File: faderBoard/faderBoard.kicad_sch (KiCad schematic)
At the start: 22 parts, among them J1 Conn_01x14_Pin, J2 Conn_01x14_Socket, U1 ADS1115IDGS

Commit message: added footprints
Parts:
- C1, C2, C3, C4, C5: footprint (none) -> Capacitor_SMD:C_0805_2012Metric_Pad1.18x1.45mm_HandSolder
- J1: footprint (none) -> Connector_PinHeader_2.54mm:PinHeader_1x14_P2.54mm_Horizontal
- J2: footprint (none) -> Connector_PinSocket_2.54mm:PinSocket_1x14_P2.54mm_Horizontal
- JP1, JP10, JP2, JP3, JP4, JP5, JP6, JP7, JP8, JP9: footprint (none) -> Jumper:SolderJumper-2_P1.3mm_Open_RoundedPad1.0x1.5mm
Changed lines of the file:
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@@
       (effects (font (size 1.27 1.27)))
     )
-    (property "Footprint" "" (at 185.42 52.07 0)
+    (property "Footprint" "Jumper:SolderJumper-2_P1.3mm_Open_RoundedPad1.0x1.5mm" (at 185.42 52.07 0)
       (effects (font (size 1.27 1.27)) hide)
     )
@@
   (symbol (lib_id "power:VCC") (at 189.23 41.91 270) (unit 1)
     (in_bom yes) (on_board yes) (dnp no) (fields_autoplaced)
-    (property "Reference" "VCC03" (at 185.42 41.91 0)
+    (property "Reference" "#VCC03" (at 185.42 41.91 0)
       (effects (font (size 1.27 1.27)) hide)
     )
@@
       (project "faderBoard"
         (path "/8d3b36b6-6263-45d8-854a-5aadc803e839"
-          (reference "VCC03") (unit 1)
+          (reference "#VCC03") (unit 1)
         )
       )
@@
       (effects (font (size 1.27 1.27)))
     )
-    (property "Footprint" "" (at 85.09 83.82 0)
+    (property "Footprint" "Jumper:SolderJumper-2_P1.3mm_Open_RoundedPad1.0x1.5mm" (at 85.09 83.82 0)
       (effects (font (size 1.27 1.27)) hide)
     )
@@
       (effects (font (size 1.27 1.27)))
     )
-    (property "Footprint" "" (at 85.09 73.66 0)
+    (property "Footprint" "Jumper:SolderJumper-2_P1.3mm_Open_RoundedPad1.0x1.5mm" (at 85.09 73.66 0)
       (effects (font (size 1.27 1.27)) hide)
     )
@@
       (effects (font (size 1.27 1.27)))
     )
-    (property "Footprint" "" (at 185.42 30.48 0)
+    (property "Footprint" "Jumper:SolderJumper-2_P1.3mm_Open_RoundedPad1.0x1.5mm" (at 185.42 30.48 0)
       (effects (font (size 1.27 1.27)) hide)
     )
@@
   (symbol (lib_id "power:VCC") (at 137.16 26.67 0) (unit 1)
     (in_bom yes) (on_board yes) (dnp no) (fields_autoplaced)
-    (property "Reference" "VCC02" (at 137.16 30.48 0)
+    (property "Reference" "#VCC02" (at 137.16 30.48 0)
       (effects (font (size 1.27 1.27)) hide)
     )
@@
       (project "faderBoard"
         (path "/8d3b36b6-6263-45d8-854a-5aadc803e839"
-          (reference "VCC02") (unit 1)
+          (reference "#VCC02") (unit 1)
         )
       )
@@
       (effects (font (size 1.27 1.27)))
     )
-    (property "Footprint" "" (at 185.42 36.83 0)
+    (property "Footprint" "Jumper:SolderJumper-2_P1.3mm_Open_RoundedPad1.0x1.5mm" (at 185.42 36.83 0)
       (effects (font (size 1.27 1.27)) hide)
     )
@@
       (effects (font (size 1.27 1.27)) (justify left))
     )
-    (property "Footprint" "" (at 194.31 101.6 0)
+    (property "Footprint" "Connector_PinSocket_2.54mm:PinSocket_1x14_P2.54mm_Horizontal" (at 194.31 101.6 0)
       (effects (font (size 1.27 1.27)) hide)
     )
@@
       (effects (font (size 1.27 1.27)) (justify left))
     )
-    (property "Footprint" "" (at 51.7652 114.3 0)
+    (property "Footprint" "Capacitor_SMD:C_0805_2012Metric_Pad1.18x1.45mm_HandSolder" (at 51.7652 114.3 0)
       (effects (font (size 1.27 1.27)) hide)
     )
@@
       (effects (font (size 1.27 1.27)))
     )
-    (property "Footprint" "" (at 185.42 41.91 0)
+    (property "Footprint" "Jumper:SolderJumper-2_P1.3mm_Open_RoundedPad1.0x1.5mm" (at 185.42 41.91 0)
       (effects (font (size 1.27 1.27)) hide)
     )
@@
       (effects (font (size 1.27 1.27)) (justify left))
     )
-    (property "Footprint" "" (at 51.7652 38.1 0)
+    (property "Footprint" "Capacitor_SMD:C_0805_2012Metric_Pad1.18x1.45mm_HandSolder" (at 51.7652 38.1 0)
       (effects (font (size 1.27 1.27)) hide)
     )
@@
   (symbol (lib_id "power:VCC") (at 38.1 43.18 0) (unit 1)
     (in_bom yes) (on_board yes) (dnp no) (fields_autoplaced)
-    (property "Reference" "VCC" (at 38.1 46.99 0)
+    (property "Reference" "#VCC0101" (at 38.1 46.99 0)
       (effects (font (size 1.27 1.27)) hide)
     )
@@
       (project "faderBoard"
         (path "/8d3b36b6-6263-45d8-854a-5aadc803e839"
-          (reference "VCC") (unit 1)
+          (reference "#VCC0101") (unit 1)
         )
       )
@@
       (effects (font (size 1.27 1.27)))
     )
-    (property "Footprint" "" (at 85.09 78.74 0)
+    (property "Footprint" "Jumper:SolderJumper-2_P1.3mm_Open_RoundedPad1.0x1.5mm" (at 85.09 78.74 0)
       (effects (font (size 1.27 1.27)) hide)
     )
@@
       (effects (font (size 1.27 1.27)))
     )
-    (property "Footprint" "" (at 158.75 101.6 0)
+    (property "Footprint" "Connector_PinHeader_2.54mm:PinHeader_1x14_P2.54mm_Horizontal" (at 158.75 101.6 0)
       (effects (font (size 1.27 1.27)) hide)
     )
@@
       (effects (font (size 1.27 1.27)))
     )
-    (property "Footprint" "" (at 85.09 88.9 0)
+    (property "Footprint" "Jumper:SolderJumper-2_P1.3mm_Open_RoundedPad1.0x1.5mm" (at 85.09 88.9 0)
       (effects (font (size 1.27 1.27)) hide)
     )
@@
       (effects (font (size 1.27 1.27)))
     )
-    (property "Footprint" "" (at 185.42 46.99 0)
+    (property "Footprint" "Jumper:SolderJumper-2_P1.3mm_Open_RoundedPad1.0x1.5mm" (at 185.42 46.99 0)
       (effects (font (size 1.27 1.27)) hide)
     )
@@
   (symbol (lib_id "power:VCC") (at 168.91 86.36 0) (unit 1)
     (in_bom yes) (on_board yes) (dnp no) (fields_autoplaced)
-    (property "Reference" "VCC01" (at 168.91 90.17 0)
+    (property "Reference" "#VCC01" (at 168.91 90.17 0)
       (effects (font (size 1.27 1.27)) hide)
     )
@@
       (project "faderBoard"
         (path "/8d3b36b6-6263-45d8-854a-5aadc803e839"
-          (reference "VCC01") (unit 1)
+          (reference "#VCC01") (unit 1)
         )
       )
@@
       (effects (font (size 1.27 1.27)) (justify left))
     )
-    (property "Footprint" "" (at 51.7652 63.5 0)
+    (property "Footprint" "Capacitor_SMD:C_0805_2012Metric_Pad1.18x1.45mm_HandSolder" (at 51.7652 63.5 0)
       (effects (font (size 1.27 1.27)) hide)
     )
@@
       (effects (font (size 1.27 1.27)) (justify left))
     )
-    (property "Footprint" "" (at 51.7652 88.9 0)
+    (property "Footprint" "Capacitor_SMD:C_0805_2012Metric_Pad1.18x1.45mm_HandSolder" (at 51.7652 88.9 0)
       (effects (font (size 1.27 1.27)) hide)
     )
@@
       (effects (font (size 1.27 1.27)))
     )
-    (property "Footprint" "" (at 185.42 25.4 0)
+    (property "Footprint" "Jumper:SolderJumper-2_P1.3mm_Open_RoundedPad1.0x1.5mm" (at 185.42 25.4 0)
       (effects (font (size 1.27 1.27)) hide)
     )
@@
       (effects (font (size 1.27 1.27)) (justify left))
     )
-    (property "Footprint" "" (at 115.2652 34.29 0)
-      (effects (font (size 1.27 1.27)) hide)
-    )
+    (property "Footprint" "Capacitor_SMD:C_0805_2012Metric_Pad1.18x1.45mm_HandSolder" (at 115.2652 34.29 0)
+      (effects (font (size 1.27 1.27)) hide)
+    )

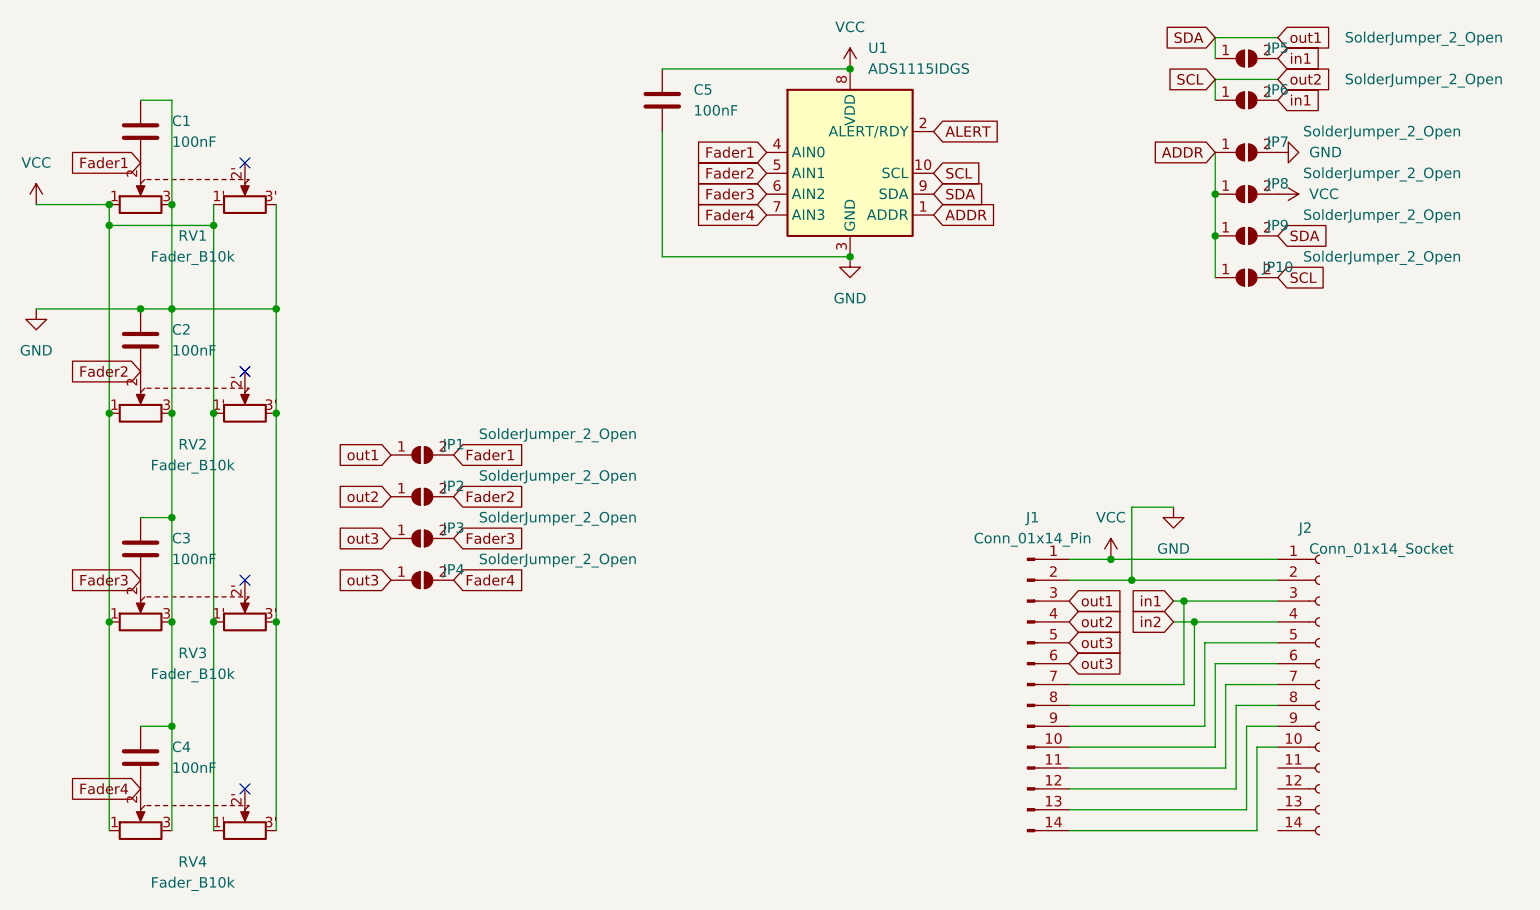
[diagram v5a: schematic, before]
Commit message: fixed pin connection
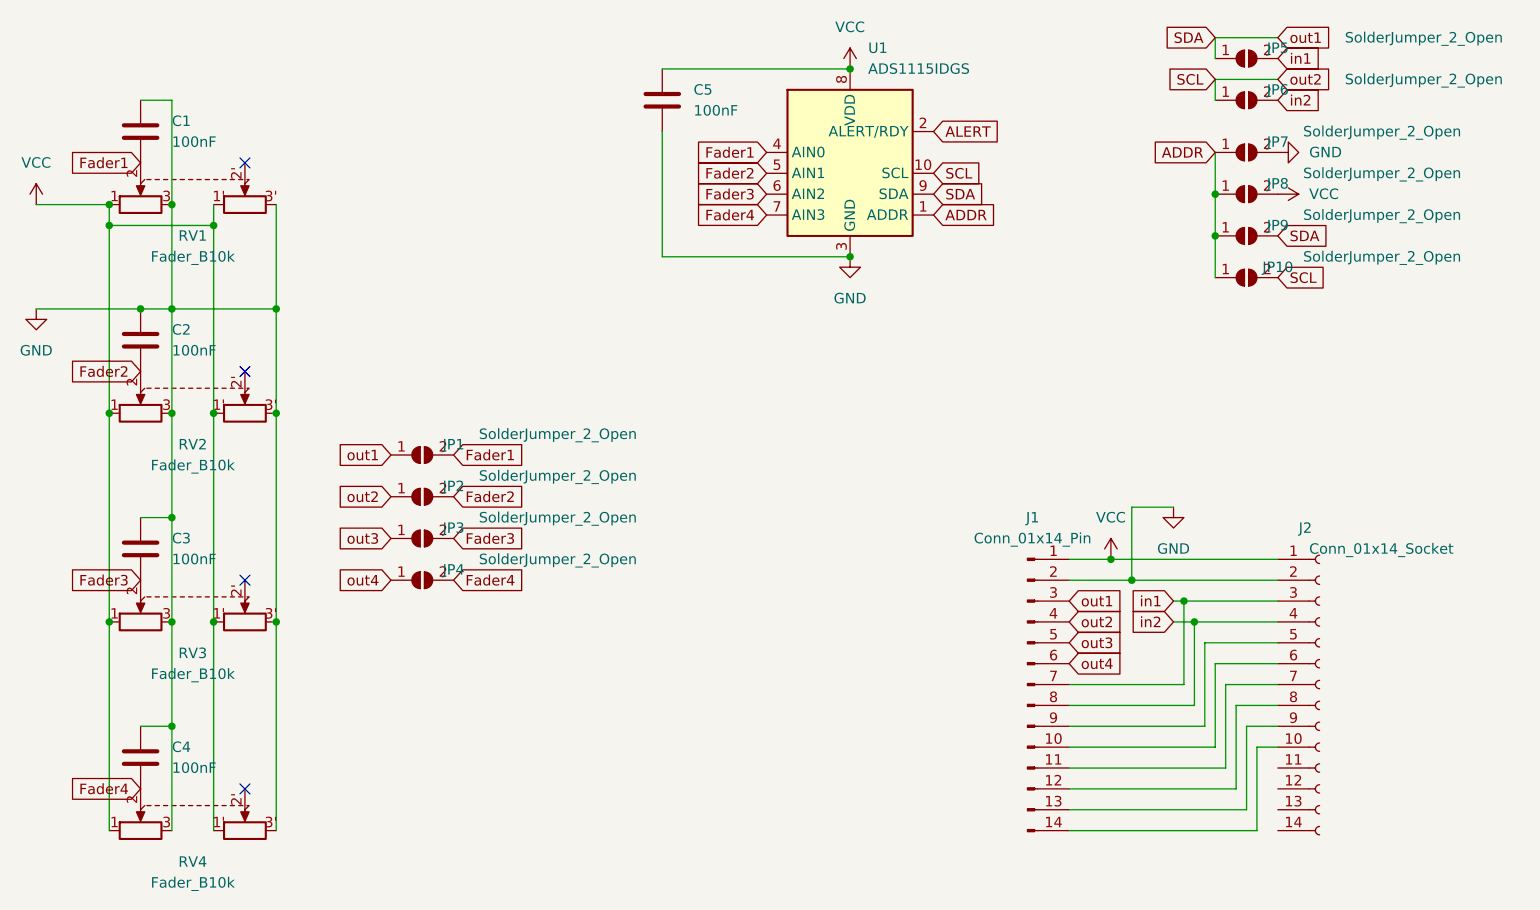
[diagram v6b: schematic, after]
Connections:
- net in1: no longer JP6.2 (B)
- net in2: now also JP6.2 (B)
- net out3: no longer J1.6 (Pin_6), JP4.1 (A)
- new net out4: J1.6 (Pin_6), JP4.1 (A)
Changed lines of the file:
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@@
     )
   )
-  (global_label "in1" (shape input) (at 189.23 30.48 0) (fields_autoplaced)
+  (global_label "in2" (shape input) (at 189.23 30.48 0) (fields_autoplaced)
     (effects (font (size 1.27 1.27)) (justify left))
     (property "Intersheetrefs" "${INTERSHEET_REFS}" (at 195.1785 30.48 0)
@@
     )
   )
-  (global_label "out3" (shape input) (at 81.28 88.9 180) (fields_autoplaced)
+  (global_label "out4" (shape input) (at 81.28 88.9 180) (fields_autoplaced)
     (effects (font (size 1.27 1.27)) (justify right))
     (property "Intersheetrefs" "${INTERSHEET_REFS}" (at 74.0616 88.9 0)
@@
     )
   )
-  (global_label "out3" (shape input) (at 163.83 99.06 0) (fields_autoplaced)
+  (global_label "out4" (shape input) (at 163.83 99.06 0) (fields_autoplaced)
     (effects (font (size 1.27 1.27)) (justify left))
     (property "Intersheetrefs" "${INTERSHEET_REFS}" (at 171.0484 99.06 0)

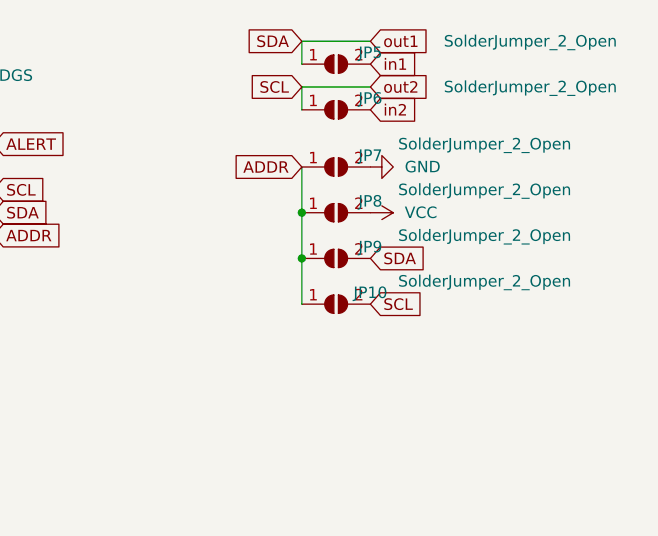
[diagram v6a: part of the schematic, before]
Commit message: connected Alert pin
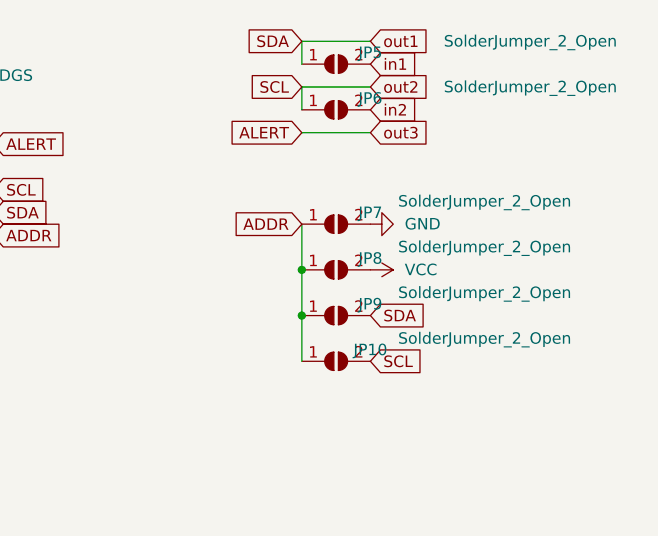
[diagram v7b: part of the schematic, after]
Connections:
- net out3 is gone; now on net ALERT: J1.5 (Pin_5), JP3.1 (A)
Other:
- moved on the sheet: JP10, JP7, JP8, JP9

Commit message: fader board small changes
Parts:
- J1: footprint Connector_PinHeader_2.54mm:PinHeader_1x14_P2.54mm_Horizontal -> Connector_PinHeader_2.54mm:PinHeader_1x14_P2.54mm_Vertical
- J2: footprint Connector_PinSocket_2.54mm:PinSocket_1x14_P2.54mm_Horizontal -> Connector_PinSocket_2.54mm:PinSocket_1x14_P2.54mm_Vertical
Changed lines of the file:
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@@
       (effects (font (size 1.27 1.27)) (justify left))
     )
-    (property "Footprint" "Connector_PinSocket_2.54mm:PinSocket_1x14_P2.54mm_Horizontal" (at 194.31 101.6 0)
+    (property "Footprint" "Connector_PinSocket_2.54mm:PinSocket_1x14_P2.54mm_Vertical" (at 194.31 101.6 0)
       (effects (font (size 1.27 1.27)) hide)
     )
@@
       (effects (font (size 1.27 1.27)))
     )
-    (property "Footprint" "Connector_PinHeader_2.54mm:PinHeader_1x14_P2.54mm_Horizontal" (at 158.75 101.6 0)
-      (effects (font (size 1.27 1.27)) hide)
-    )
+    (property "Footprint" "Connector_PinHeader_2.54mm:PinHeader_1x14_P2.54mm_Vertical" (at 158.75 101.6 0)
+      (effects (font (size 1.27 1.27)) hide)
+    )
